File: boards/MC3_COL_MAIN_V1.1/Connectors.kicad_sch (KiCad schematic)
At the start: 11 parts, among them J13 HARNESS_FFC_6P, J3 ENC_leaf1, J4 ENC_leaf2, J5 ENC_leaf3, J6 ENC_leaf4

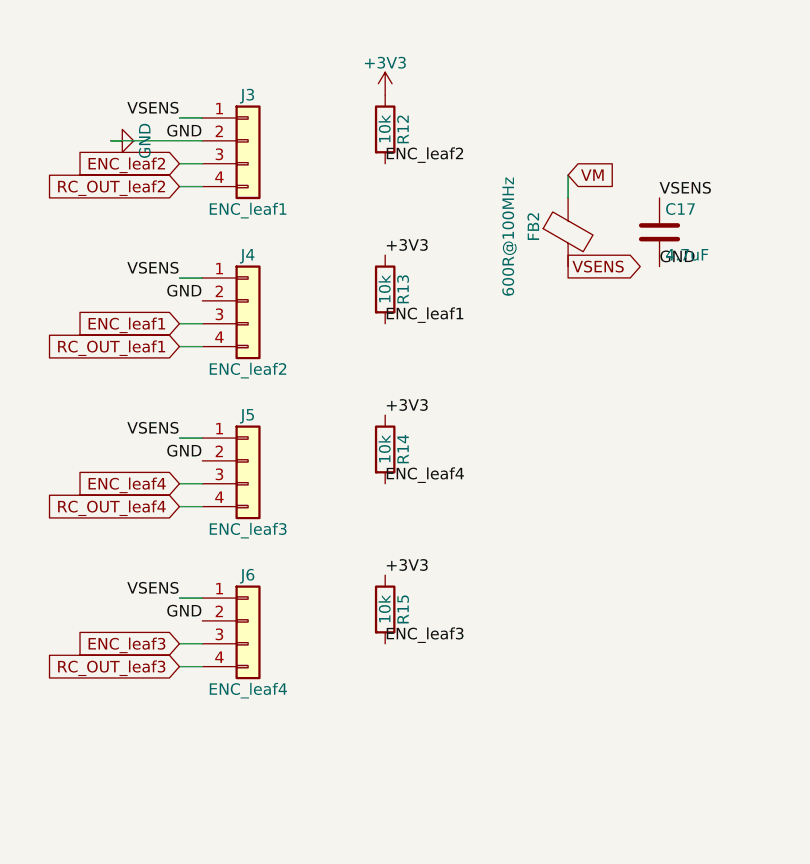
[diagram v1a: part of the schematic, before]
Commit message: Schematic readability pass: Connectors names fixed, Power chains, field tidy
- Connectors: J3-J6 Value fields finally match their post-swap nets
  (J3=ENC_leaf2, J4=ENC_leaf1, J5=ENC_leaf4, J6=ENC_leaf3) - they had kept
  their pre-14c identities; FB2 value text reset to its library anchor.
- Power committed previously: protection + LDO redrawn as wired chains.
- Netlist verified byte-identical to the pre-pass baseline; ERC 0 errors.

Co-Authored-By: Claude Fable 5 <noreply@anthropic.com>
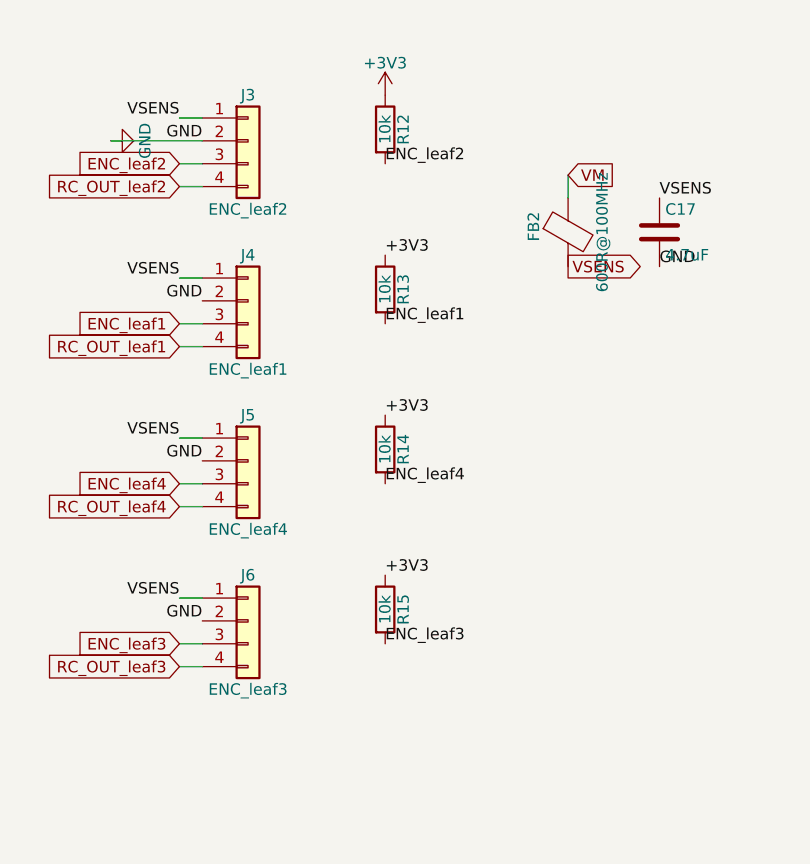
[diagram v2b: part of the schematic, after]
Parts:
- J3: value ENC_leaf1 -> ENC_leaf2
- J4: value ENC_leaf2 -> ENC_leaf1
- J5: value ENC_leaf3 -> ENC_leaf4
- J6: value ENC_leaf4 -> ENC_leaf3
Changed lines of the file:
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@@
 	(generator_version "10.0")
 	(paper "A4")
-	(text "Review 2026-08-22: FFC VIN now from VSENS = VM filtered by FB61 + C63."
-		(exclude_from_sim no)
-		(at 30 195 0)
-		(effects
-			(font
-				(size 1.5 1.5)
-			)
-		)
-	)
-	(text "Encoder interface - four 0.5 mm FFCs, one per leaf, to the LX34311 sensor boards (COL-COTS-0016). Contract: VIN 4-6 V from VM, GND, SIG open-drain pulled to +3V3 here (10k), spare unassigned. Vault: Main-Board-01 Encoder Interface / Connectors. Motor pads are on the MotorChannel sheet; supply pads on Power."
-		(exclude_from_sim no)
-		(at 30 25 0)
-		(effects
-			(font
-				(size 1.5 1.5)
-			)
-		)
-	)
 	(wire
 		(pts
-			(xy 54.61 107.95) (xy 52.07 107.95)
+			(xy 54.61 107.95)
+			(xy 52.07 107.95)
 		)
 		(stroke
@@
 	(wire
 		(pts
-			(xy 147.32 66.04) (xy 144.78 66.04)
+			(xy 147.32 66.04)
+			(xy 144.78 66.04)
 		)
 		(stroke
@@
 	(wire
 		(pts
-			(xy 54.61 49.53) (xy 44.45 49.53)
+			(xy 54.61 49.53)
+			(xy 44.45 49.53)
 		)
 		(stroke
@@
 	(wire
 		(pts
-			(xy 54.61 82.55) (xy 52.07 82.55)
+			(xy 54.61 82.55)
+			(xy 52.07 82.55)
 		)
 		(stroke
@@
 	(wire
 		(pts
-			(xy 147.32 60.96) (xy 144.78 60.96)
+			(xy 147.32 60.96)
+			(xy 144.78 60.96)
 		)
 		(stroke
@@
 	(wire
 		(pts
-			(xy 54.61 52.07) (xy 52.07 52.07)
+			(xy 54.61 52.07)
+			(xy 52.07 52.07)
 		)
 		(stroke
@@
 	(wire
 		(pts
-			(xy 147.32 58.42) (xy 144.78 58.42)
+			(xy 147.32 58.42)
+			(xy 144.78 58.42)
 		)
 		(stroke
@@
 	(wire
 		(pts
-			(xy 147.32 68.58) (xy 144.78 68.58)
+			(xy 147.32 68.58)
+			(xy 144.78 68.58)
 		)
 		(stroke
@@
 	(wire
 		(pts
-			(xy 54.61 90.17) (xy 52.07 90.17)
+			(xy 54.61 90.17)
+			(xy 52.07 90.17)
 		)
 		(stroke
@@
 	(wire
 		(pts
-			(xy 54.61 64.77) (xy 52.07 64.77)
+			(xy 54.61 64.77)
+			(xy 52.07 64.77)
 		)
 		(stroke
@@
 	(wire
 		(pts
-			(xy 95.25 55.88) (xy 95.25 53.34)
+			(xy 95.25 55.88)
+			(xy 95.25 53.34)
 		)
 		(stroke
@@
 	(wire
 		(pts
-			(xy 54.61 54.61) (xy 52.07 54.61)
+			(xy 54.61 54.61)
+			(xy 52.07 54.61)
 		)
 		(stroke
@@
 	(wire
 		(pts
-			(xy 147.32 63.5) (xy 144.78 63.5)
+			(xy 147.32 63.5)
+			(xy 144.78 63.5)
 		)
 		(stroke
@@
 	(wire
 		(pts
-			(xy 54.61 100.33) (xy 52.07 100.33)
+			(xy 54.61 100.33)
+			(xy 52.07 100.33)
 		)
 		(stroke
@@
 	(wire
 		(pts
-			(xy 54.61 87.63) (xy 52.07 87.63)
+			(xy 54.61 87.63)
+			(xy 52.07 87.63)
 		)
 		(stroke
@@
 	(wire
 		(pts
-			(xy 54.61 69.85) (xy 52.07 69.85)
+			(xy 54.61 69.85)
+			(xy 52.07 69.85)
 		)
 		(stroke
@@
 	(wire
 		(pts
-			(xy 54.61 72.39) (xy 52.07 72.39)
+			(xy 54.61 72.39)
+			(xy 52.07 72.39)
 		)
 		(stroke
@@
 	(wire
 		(pts
-			(xy 54.61 105.41) (xy 52.07 105.41)
+			(xy 54.61 105.41)
+			(xy 52.07 105.41)
 		)
 		(stroke
@@
 	(wire
 		(pts
-			(xy 54.61 46.99) (xy 52.07 46.99)
+			(xy 54.61 46.99)
+			(xy 52.07 46.99)
 		)
 		(stroke
@@
 	(wire
 		(pts
-			(xy 147.32 71.12) (xy 144.78 71.12)
+			(xy 147.32 71.12)
+			(xy 144.78 71.12)
 		)
 		(stroke
 			(width 0)
 			(type default)
+		)
+	)
+	(text "Review 2026-08-22: FFC VIN now from VSENS = VM filtered by FB61 + C63."
+		(at 30 195 0)
+		(effects
+			(font
+				(size 1.5 1.5)
+			)
+		)
+	)
+	(text "Encoder interface - four 0.5 mm FFCs, one per leaf, to the LX34311 sensor boards (COL-COTS-0016). Contract: VIN 4-6 V from VM, GND, SIG open-drain pulled to +3V3 here (10k), spare unassigned. Vault: Main-Board-01 Encoder Interface / Connectors. Motor pads are on the MotorChannel sheet; supply pads on Power."
+		(at 30 25 0)
+		(effects
+			(font
+				(size 1.5 1.5)
+			)
 		)
 	)
@@
 		(at 59.69 49.53 0)
 		(unit 1)
-		(body_style 1)
 		(exclude_from_sim no)
 		(in_bom yes)
 		(on_board yes)
-		(in_pos_files yes)
 		(dnp no)
 		(property "Reference" "J3"
@@
 			)
 		)
-		(property "Value" "ENC_leaf1"
+		(property "Value" "ENC_leaf2"
 			(at 59.69 57.15 0)
 			(show_name no)
@@
 			)
 		)
+		(body_style 1)
+		(in_pos_files yes)
 		(pin "2"
 		)
@@
 		(at 44.45 49.53 90)
 		(unit 1)
-		(body_style 1)
 		(exclude_from_sim no)
 		(in_bom yes)
 		(on_board yes)
-		(in_pos_files yes)
 		(dnp no)
 		(property "Reference" "#PWR09"
@@
 			)
 		)
+		(body_style 1)
+		(in_pos_files yes)
 		(pin "1"
 		)
@@
 		(at 59.69 102.87 0)
 		(unit 1)
-		(body_style 1)
 		(exclude_from_sim no)
 		(in_bom yes)
 		(on_board yes)
-		(in_pos_files yes)
 		(dnp no)
 		(property "Reference" "J6"
@@
 			)
 		)
-		(property "Value" "ENC_leaf4"
+		(property "Value" "ENC_leaf3"
 			(at 59.69 110.49 0)
 			(show_name no)
@@
 			)
 		)
+		(body_style 1)
+		(in_pos_files yes)
 		(pin "2"
 		)
@@
 		(at 74.93 44.45 0)
 		(unit 1)
-		(body_style 1)
 		(exclude_from_sim no)
 		(in_bom yes)
 		(on_board yes)
-		(in_pos_files yes)
 		(dnp no)
 		(property "Reference" "#PWR010"
@@
 			)
 		)
+		(body_style 1)
+		(in_pos_files yes)
 		(pin "1"
 		)
@@
 		(at 74.93 66.04 0)
 		(unit 1)
-		(body_style 1)
 		(exclude_from_sim no)
 		(in_bom yes)
 		(on_board yes)
-		(in_pos_files yes)
 		(dnp no)
 		(property "Reference" "R13"
@@
 			)
 		)
+		(body_style 1)
+		(in_pos_files yes)
 		(pin "1"
 		)
@@
 		(at 74.93 101.6 0)
 		(unit 1)
-		(body_style 1)
 		(exclude_from_sim no)
 		(in_bom yes)
 		(on_board yes)
-		(in_pos_files yes)
 		(dnp no)
 		(property "Reference" "R15"
@@
 			)
 		)
+		(body_style 1)
+		(in_pos_files yes)
 		(pin "1"
 		)
@@
 		(at 105.41 59.69 0)
 		(unit 1)
-		(body_style 1)
 		(exclude_from_sim no)
 		(in_bom yes)
 		(on_board yes)
-		(in_pos_files yes)
 		(dnp no)
 		(property "Reference" "C17"
@@
 			)
 		)
+		(body_style 1)
+		(in_pos_files yes)
 		(pin "1"
 		)
@@
 		(at 59.69 67.31 0)
 		(unit 1)
-		(body_style 1)
 		(exclude_from_sim no)
 		(in_bom yes)
 		(on_board yes)
-		(in_pos_files yes)
 		(dnp no)
 		(property "Reference" "J4"
@@
 			)
 		)
-		(property "Value" "ENC_leaf2"
+		(property "Value" "ENC_leaf1"
 			(at 59.69 74.93 0)
 			(show_name no)
@@
 			)
 		)
+		(body_style 1)
+		(in_pos_files yes)
 		(pin "3"
 		)
@@
 		(at 59.69 85.09 0)
 		(unit 1)
-		(body_style 1)
 		(exclude_from_sim no)
 		(in_bom yes)
 		(on_board yes)
-		(in_pos_files yes)
 		(dnp no)
 		(property "Reference" "J5"
@@
 			)
 		)
-		(property "Value" "ENC_leaf3"
+		(property "Value" "ENC_leaf4"
 			(at 59.69 92.71 0)
 			(show_name no)
@@
 			)
 		)
+		(body_style 1)
+		(in_pos_files yes)
 		(pin "4"
 		)
@@
 		(at 95.25 59.69 0)
 		(unit 1)
-		(body_style 1)
 		(exclude_from_sim no)
 		(in_bom yes)
 		(on_board yes)
-		(in_pos_files yes)
 		(dnp no)
 		(property "Reference" "FB2"
@@
 		)
 		(property "Value" "600R@100MHz"
-			(at 88.646 60.198 90)
+			(at 99.06 59.69 90)
 			(show_name no)
 			(do_not_autoplace no)
@@
 			)
 		)
+		(body_style 1)
+		(in_pos_files yes)
 		(pin "2"
 		)
@@
 		(at 152.4 63.5 0)
 		(unit 1)
-		(body_style 1)
 		(exclude_from_sim no)
 		(in_bom yes)
 		(on_board yes)
-		(in_pos_files yes)
 		(dnp no)
 		(property "Reference" "J13"
@@
 			)
 		)
+		(body_style 1)
+		(in_pos_files yes)
 		(pin "4"
 		)
@@
 		(at 74.93 48.26 0)
 		(unit 1)
-		(body_style 1)
 		(exclude_from_sim no)
 		(in_bom yes)
 		(on_board yes)
-		(in_pos_files yes)
 		(dnp no)
 		(property "Reference" "R12"
@@
 			)
 		)
+		(body_style 1)
+		(in_pos_files yes)
 		(pin "1"
 		)
@@
 		(at 74.93 83.82 0)
 		(unit 1)
-		(body_style 1)
 		(exclude_from_sim no)
 		(in_bom yes)
 		(on_board yes)
-		(in_pos_files yes)
 		(dnp no)
 		(property "Reference" "R14"
@@
 			)
 		)
+		(body_style 1)
+		(in_pos_files yes)
 		(pin "1"
 		)

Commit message: V1.1 schematics: per-instance Description fields on ~63 symbols
The component-docs Role source of record. Netlist unchanged, ERC 0.

Co-Authored-By: Claude Fable 5 <noreply@anthropic.com>
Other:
- note removed: "Encoder interface - four 0.5 mm FFCs, one per leaf, to the LX34311 sensor boards (COL-COTS-0016). Contract: VIN 4-6 V from VM, GND, SIG open-drain pulled to +3V3 here (10k), spare unassigned. Vault: Main-Board-01 Encoder Interface / Connectors. Motor pads are on the MotorChannel sheet; supply pads on Power."
- note removed: "Review 2026-08-22: FFC VIN now from VSENS = VM filtered by FB61 + C63."
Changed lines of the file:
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@@
 	(wire
 		(pts
-			(xy 54.61 107.95)
-			(xy 52.07 107.95)
+			(xy 54.61 107.95) (xy 52.07 107.95)
 		)
 		(stroke
@@
 	(wire
 		(pts
-			(xy 147.32 66.04)
-			(xy 144.78 66.04)
+			(xy 147.32 66.04) (xy 144.78 66.04)
 		)
 		(stroke
@@
 	(wire
 		(pts
-			(xy 54.61 49.53)
-			(xy 44.45 49.53)
+			(xy 54.61 49.53) (xy 44.45 49.53)
 		)
 		(stroke
@@
 	(wire
 		(pts
-			(xy 54.61 82.55)
-			(xy 52.07 82.55)
+			(xy 54.61 82.55) (xy 52.07 82.55)
 		)
 		(stroke
@@
 	(wire
 		(pts
-			(xy 147.32 60.96)
-			(xy 144.78 60.96)
+			(xy 147.32 60.96) (xy 144.78 60.96)
 		)
 		(stroke
@@
 	(wire
 		(pts
-			(xy 54.61 52.07)
-			(xy 52.07 52.07)
+			(xy 54.61 52.07) (xy 52.07 52.07)
 		)
 		(stroke
@@
 	(wire
 		(pts
-			(xy 147.32 58.42)
-			(xy 144.78 58.42)
+			(xy 147.32 58.42) (xy 144.78 58.42)
 		)
 		(stroke
@@
 	(wire
 		(pts
-			(xy 147.32 68.58)
-			(xy 144.78 68.58)
+			(xy 147.32 68.58) (xy 144.78 68.58)
 		)
 		(stroke
@@
 	(wire
 		(pts
-			(xy 54.61 90.17)
-			(xy 52.07 90.17)
+			(xy 54.61 90.17) (xy 52.07 90.17)
 		)
 		(stroke
@@
 	(wire
 		(pts
-			(xy 54.61 64.77)
-			(xy 52.07 64.77)
+			(xy 54.61 64.77) (xy 52.07 64.77)
 		)
 		(stroke
@@
 	(wire
 		(pts
-			(xy 95.25 55.88)
-			(xy 95.25 53.34)
+			(xy 95.25 55.88) (xy 95.25 53.34)
 		)
 		(stroke
@@
 	(wire
 		(pts
-			(xy 54.61 54.61)
-			(xy 52.07 54.61)
+			(xy 54.61 54.61) (xy 52.07 54.61)
 		)
 		(stroke
@@
 	(wire
 		(pts
-			(xy 147.32 63.5)
-			(xy 144.78 63.5)
+			(xy 147.32 63.5) (xy 144.78 63.5)
 		)
 		(stroke
@@
 	(wire
 		(pts
-			(xy 54.61 100.33)
-			(xy 52.07 100.33)
+			(xy 54.61 100.33) (xy 52.07 100.33)
 		)
 		(stroke
@@
 	(wire
 		(pts
-			(xy 54.61 87.63)
-			(xy 52.07 87.63)
+			(xy 54.61 87.63) (xy 52.07 87.63)
 		)
 		(stroke
@@
 	(wire
 		(pts
-			(xy 54.61 69.85)
-			(xy 52.07 69.85)
+			(xy 54.61 69.85) (xy 52.07 69.85)
 		)
 		(stroke
@@
 	(wire
 		(pts
-			(xy 54.61 72.39)
-			(xy 52.07 72.39)
+			(xy 54.61 72.39) (xy 52.07 72.39)
 		)
 		(stroke
@@
 	(wire
 		(pts
-			(xy 54.61 105.41)
-			(xy 52.07 105.41)
+			(xy 54.61 105.41) (xy 52.07 105.41)
 		)
 		(stroke
@@
 	(wire
 		(pts
-			(xy 54.61 46.99)
-			(xy 52.07 46.99)
+			(xy 54.61 46.99) (xy 52.07 46.99)
 		)
 		(stroke
@@
 	(wire
 		(pts
-			(xy 147.32 71.12)
-			(xy 144.78 71.12)
+			(xy 147.32 71.12) (xy 144.78 71.12)
 		)
 		(stroke
 			(width 0)
 			(type default)
-		)
-	)
-	(text "Review 2026-08-22: FFC VIN now from VSENS = VM filtered by FB61 + C63."
-		(at 30 195 0)
-		(effects
-			(font
-				(size 1.5 1.5)
-			)
-		)
-	)
-	(text "Encoder interface - four 0.5 mm FFCs, one per leaf, to the LX34311 sensor boards (COL-COTS-0016). Contract: VIN 4-6 V from VM, GND, SIG open-drain pulled to +3V3 here (10k), spare unassigned. Vault: Main-Board-01 Encoder Interface / Connectors. Motor pads are on the MotorChannel sheet; supply pads on Power."
-		(at 30 25 0)
-		(effects
-			(font
-				(size 1.5 1.5)
-			)
 		)
 	)
@@
 		(at 59.69 49.53 0)
 		(unit 1)
+		(body_style 1)
 		(exclude_from_sim no)
 		(in_bom yes)
 		(on_board yes)
+		(in_pos_files yes)
 		(dnp no)
 		(property "Reference" "J3"
@@
 			)
 		)
-		(property "Description" ""
+		(property "Description" "Leaf 2 encoder FFC ([[COL-COTS-0031]] AYF530435, 0.5 mm 4-way): VSENS / GND / SIG / RC_OUT share — see [[Main-Board-01 Encoder Interface]]."
 			(at 59.69 49.53 0)
 			(show_name no)
@@
 			)
 		)
-		(body_style 1)
-		(in_pos_files yes)
 		(pin "2"
 		)
@@
 		(at 44.45 49.53 90)
 		(unit 1)
+		(body_style 1)
 		(exclude_from_sim no)
 		(in_bom yes)
 		(on_board yes)
+		(in_pos_files yes)
 		(dnp no)
 		(property "Reference" "#PWR09"
@@
 			)
 		)
-		(body_style 1)
-		(in_pos_files yes)
 		(pin "1"
 		)
@@
 		(at 59.69 102.87 0)
 		(unit 1)
+		(body_style 1)
 		(exclude_from_sim no)
 		(in_bom yes)
 		(on_board yes)
+		(in_pos_files yes)
 		(dnp no)
 		(property "Reference" "J6"
@@
 			)
 		)
-		(property "Description" ""
+		(property "Description" "Leaf 3 encoder FFC ([[COL-COTS-0031]]): VSENS / GND / SIG / RC_OUT share."
 			(at 59.69 102.87 0)
 			(show_name no)
@@
 			)
 		)
-		(body_style 1)
-		(in_pos_files yes)
 		(pin "2"
 		)
@@
 		(at 74.93 44.45 0)
 		(unit 1)
+		(body_style 1)
 		(exclude_from_sim no)
 		(in_bom yes)
 		(on_board yes)
+		(in_pos_files yes)
 		(dnp no)
 		(property "Reference" "#PWR010"
@@
 			)
 		)
-		(body_style 1)
-		(in_pos_files yes)
 		(pin "1"
 		)
@@
 		(at 74.93 66.04 0)
 		(unit 1)
+		(body_style 1)
 		(exclude_from_sim no)
 		(in_bom yes)
 		(on_board yes)
+		(in_pos_files yes)
 		(dnp no)
 		(property "Reference" "R13"
@@
 			)
 		)
-		(body_style 1)
-		(in_pos_files yes)
 		(pin "1"
 		)
@@
 		(at 74.93 101.6 0)
 		(unit 1)
+		(body_style 1)
 		(exclude_from_sim no)
 		(in_bom yes)
 		(on_board yes)
+		(in_pos_files yes)
 		(dnp no)
 		(property "Reference" "R15"
@@
 			)
 		)
-		(body_style 1)
-		(in_pos_files yes)
 		(pin "1"
 		)
@@
 		(at 105.41 59.69 0)
 		(unit 1)
+		(body_style 1)
 		(exclude_from_sim no)
 		(in_bom yes)
 		(on_board yes)
+		(in_pos_files yes)
 		(dnp no)
 		(property "Reference" "C17"
@@
 			)
 		)
-		(property "Description" ""
+		(property "Description" "VSENS rail cap 4.7 µF — one cap serves all four encoder connectors (#tbd per-connector 100 nF owed)."
 			(at 105.41 59.69 0)
 			(show_name no)
@@
 			)
 		)
-		(body_style 1)
-		(in_pos_files yes)
 		(pin "1"
 		)
@@
 		(at 59.69 67.31 0)
 		(unit 1)
+		(body_style 1)
 		(exclude_from_sim no)
 		(in_bom yes)
 		(on_board yes)
+		(in_pos_files yes)
 		(dnp no)
 		(property "Reference" "J4"
@@
 			)
 		)
-		(property "Description" ""
+		(property "Description" "Leaf 1 encoder FFC ([[COL-COTS-0031]]): VSENS / GND / SIG / RC_OUT share."
 			(at 59.69 67.31 0)
 			(show_name no)
@@
 			)
 		)
-		(body_style 1)
-		(in_pos_files yes)
 		(pin "3"
 		)
@@
 		(at 59.69 85.09 0)
 		(unit 1)
+		(body_style 1)
 		(exclude_from_sim no)
 		(in_bom yes)
 		(on_board yes)
+		(in_pos_files yes)
 		(dnp no)
 		(property "Reference" "J5"
@@
 			)
 		)
-		(property "Description" ""
+		(property "Description" "Leaf 4 encoder FFC ([[COL-COTS-0031]]): VSENS / GND / SIG / RC_OUT share."
 			(at 59.69 85.09 0)
 			(show_name no)
@@
 			)
 		)
-		(body_style 1)
-		(in_pos_files yes)
 		(pin "4"
 		)
@@
 		(at 95.25 59.69 0)
 		(unit 1)
+		(body_style 1)
 		(exclude_from_sim no)
 		(in_bom yes)
 		(on_board yes)
+		(in_pos_files yes)
 		(dnp no)
 		(property "Reference" "FB2"
@@
 			)
 		)
-		(property "Description" ""
+		(property "Description" "VSENS feed bead from VM (600 Ω @ 100 MHz) — the encoder supply filter."
 			(at 95.25 59.69 0)
 			(show_name no)
@@
 			)
 		)
-		(body_style 1)
-		(in_pos_files yes)
 		(pin "2"
 		)
@@
 		(at 152.4 63.5 0)
 		(unit 1)
+		(body_style 1)
 		(exclude_from_sim no)
 		(in_bom yes)
 		(on_board yes)
+		(in_pos_files yes)
 		(dnp no)
 		(property "Reference" "J13"
@@
 			)
 		)
-		(property "Description" ""
+		(property "Description" "The machine harness connector [[COL-COTS-0041]] TE 84952-6 (1.0 mm 6-way FPC, ZIF, underside): 24 V supply, CAN, and the yaw motor pair on one flat cable."
 			(at 152.4 63.5 0)
 			(show_name no)
@@
 			)
 		)
-		(body_style 1)
-		(in_pos_files yes)
 		(pin "4"
 		)
@@
 		(at 74.93 48.26 0)
 		(unit 1)
+		(body_style 1)
 		(exclude_from_sim no)
 		(in_bom yes)
 		(on_board yes)
+		(in_pos_files yes)
 		(dnp no)
 		(property "Reference" "R12"
@@
 			)
 		)
-		(body_style 1)
-		(in_pos_files yes)
 		(pin "1"
 		)
@@
 		(at 74.93 83.82 0)
 		(unit 1)
+		(body_style 1)
 		(exclude_from_sim no)
 		(in_bom yes)
 		(on_board yes)
+		(in_pos_files yes)
 		(dnp no)
 		(property "Reference" "R14"
@@
 			)
 		)
-		(body_style 1)
-		(in_pos_files yes)
 		(pin "1"
 		)
